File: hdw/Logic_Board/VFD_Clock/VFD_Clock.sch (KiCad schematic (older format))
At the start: 0 parts

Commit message: More work, project restructuring
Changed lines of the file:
@@
 $Descr A 11000 8500
 encoding utf-8
-Sheet 1 14
-Title ""
-Date ""
-Rev ""
-Comp ""
+Sheet 1 19
+Title "VFD Clock"
+Date "2019-04-11"
+Rev "A"
+Comp "Drew Maatman"
 Comment1 ""
 Comment2 ""
@@
 $EndSheet
 $Sheet
-S 3690 4410 500  150
+S 3690 4380 500  150
 U 5B3E071A
 F0 "Temperature Sensors" 50
@@
 F1 "POS24_Input.sch" 50
 $EndSheet
+$Sheet
+S 1180 2600 500  150
+U 5CB0BC26
+F0 "Microcontroller Programming" 50
+F1 "Microcontroller_Programming.sch" 50
+$EndSheet
+$Sheet
+S 3690 2930 500  150
+U 5CB7A8BC
+F0 "Status LEDs" 50
+F1 "Status_LEDs.sch" 50
+$EndSheet
+$Sheet
+S 3690 3280 500  150
+U 5CB7A8C3
+F0 "PGOOD LEDs" 50
+F1 "PGOOD_LEDs.sch" 50
+$EndSheet
+$Sheet
+S 6400 4510 500  150
+U 5CB7B79E
+F0 "IO_Connectors" 50
+F1 "IO_Connectors.sch" 50
+$EndSheet
+$Sheet
+S 6400 4860 500  150
+U 5CB8A16A
+F0 "IO Buffers" 50
+F1 "IO_Buffers.sch" 50
+$EndSheet
 $EndSCHEMATC

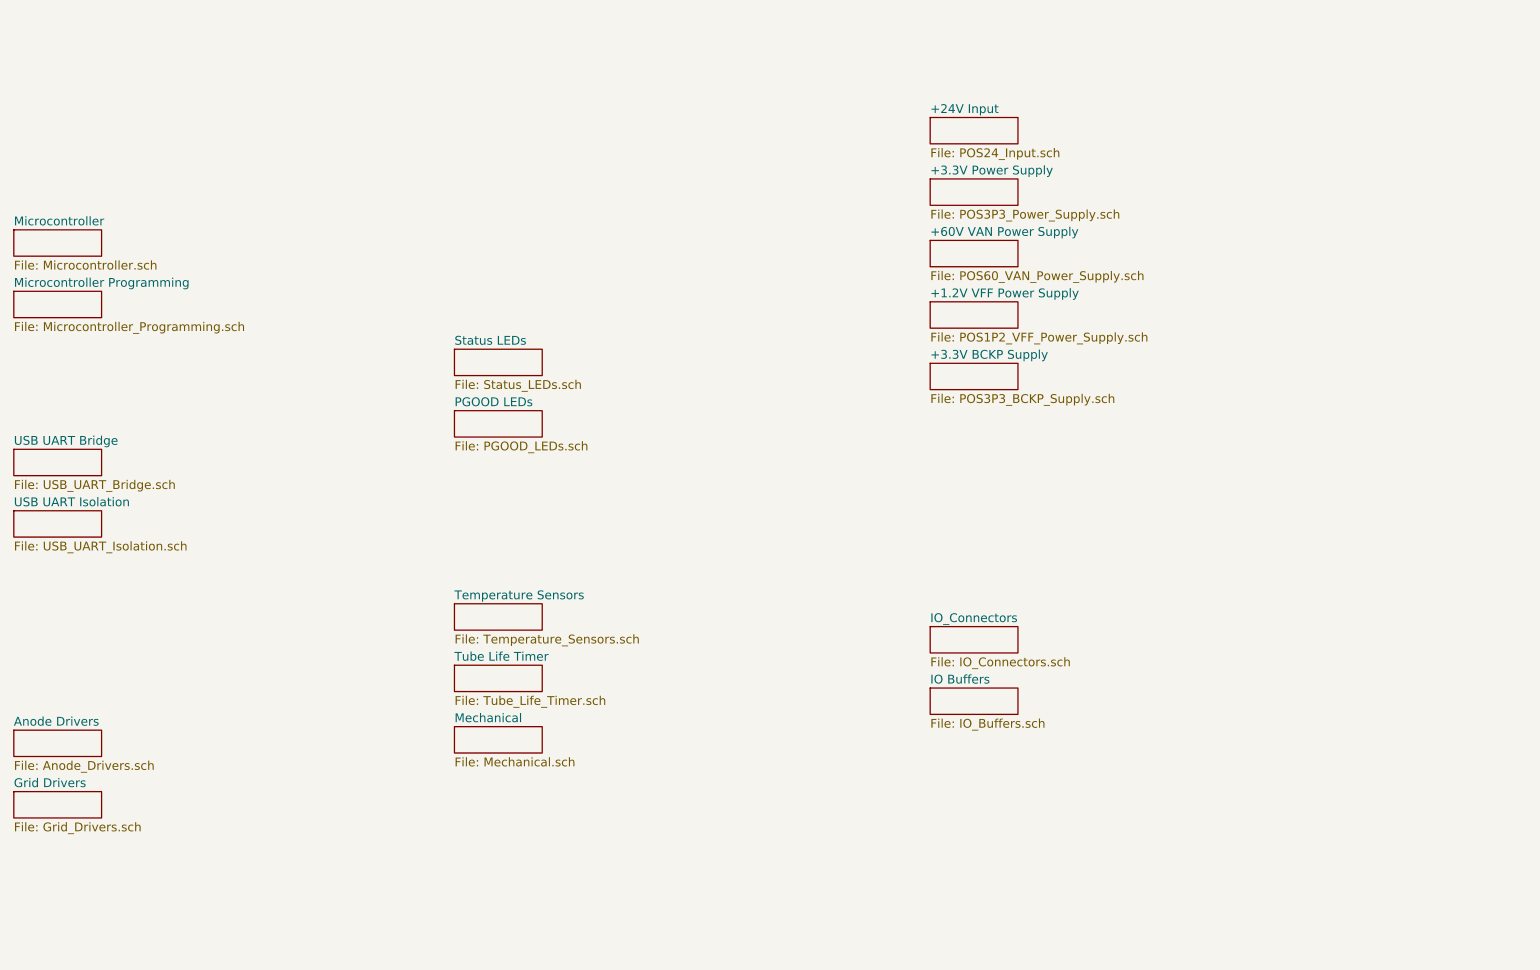
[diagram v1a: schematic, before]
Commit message: Added display board schematic, other additions to logic board
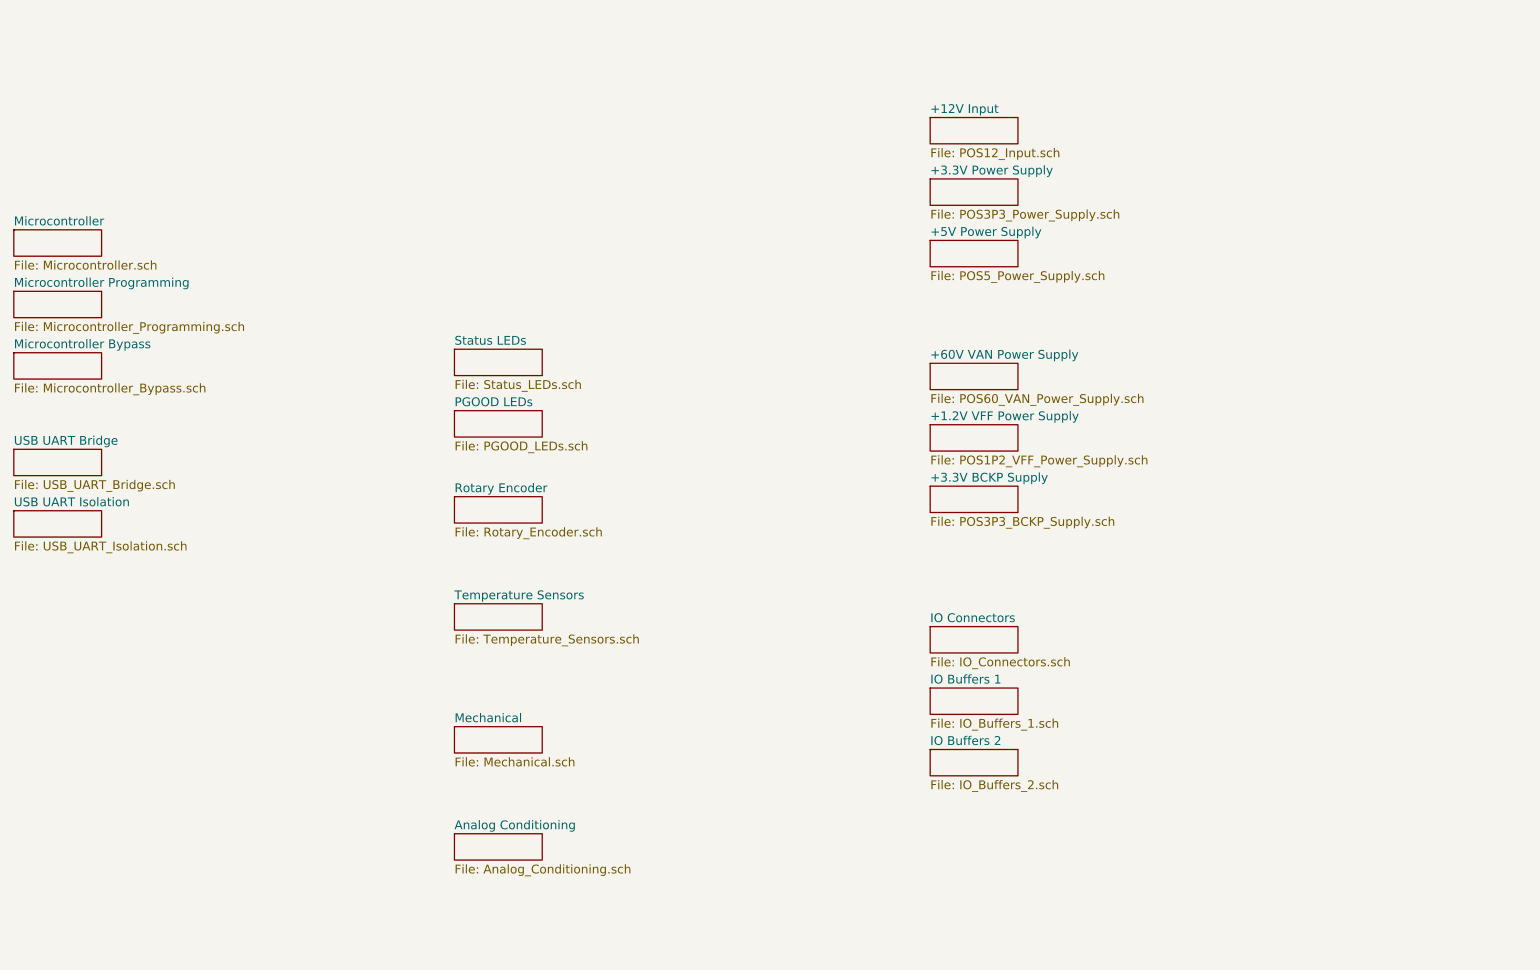
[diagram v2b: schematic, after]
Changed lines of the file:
@@
 $Descr A 11000 8500
 encoding utf-8
-Sheet 1 19
+Sheet 1 21
 Title "VFD Clock"
 Date "2019-04-11"
@@
 $EndSheet
 $Sheet
-S 6400 1960 500  150
-U 5A0B00BA
-F0 "+3.3V Power Supply" 50
-F1 "POS3P3_Power_Supply.sch" 50
-$EndSheet
-$Sheet
-S 6400 2310 500  150
+S 6400 3010 500  150
 U 5A0BC776
 F0 "+60V VAN Power Supply" 50
@@
 $EndSheet
 $Sheet
-S 6400 2660 500  150
+S 6400 3360 500  150
 U 5A0A7E5F
 F0 "+1.2V VFF Power Supply" 50
 F1 "POS1P2_VFF_Power_Supply.sch" 50
-$EndSheet
-$Sheet
-S 1180 5100 500  150
-U 5A2D2FD2
-F0 "Anode Drivers" 50
-F1 "Anode_Drivers.sch" 50
-$EndSheet
-$Sheet
-S 1180 5450 500  150
-U 5A2E3925
-F0 "Grid Drivers" 50
-F1 "Grid_Drivers.sch" 50
 $EndSheet
 $Sheet
@@
 $EndSheet
 $Sheet
-S 3690 4730 500  150
-U 5B4B0915
-F0 "Tube Life Timer" 50
-F1 "Tube_Life_Timer.sch" 50
-$EndSheet
-$Sheet
 S 3690 5080 500  150
 U 5B583C3D
@@
 $EndSheet
 $Sheet
-S 6400 3010 500  150
+S 6400 3710 500  150
 U 5A557C58
 F0 "+3.3V BCKP Supply" 50
@@
 F0 "USB UART Isolation" 50
 F1 "USB_UART_Isolation.sch" 50
-$EndSheet
-$Sheet
-S 6400 1610 500  150
-U 5CB364CC
-F0 "+24V Input" 50
-F1 "POS24_Input.sch" 50
 $EndSheet
 $Sheet
@@
 S 6400 4510 500  150
 U 5CB7B79E
-F0 "IO_Connectors" 50
+F0 "IO Connectors" 50
 F1 "IO_Connectors.sch" 50
 $EndSheet
@@
 S 6400 4860 500  150
 U 5CB8A16A
-F0 "IO Buffers" 50
-F1 "IO_Buffers.sch" 50
+F0 "IO Buffers 1" 50
+F1 "IO_Buffers_1.sch" 50
+$EndSheet
+$Sheet
+S 1180 2950 500  150
+U 5CB25152
+F0 "Microcontroller Bypass" 50
+F1 "Microcontroller_Bypass.sch" 50
+$EndSheet
+$Sheet
+S 6400 1610 500  150
+U 5CB6F1ED
+F0 "+12V Input" 50
+F1 "POS12_Input.sch" 50
+$EndSheet
+$Sheet
+S 6400 1960 500  150
+U 5CB7718D
+F0 "+3.3V Power Supply" 50
+F1 "POS3P3_Power_Supply.sch" 50
+$EndSheet
+$Sheet
+S 3690 3770 500  150
+U 5CC7D654
+F0 "Rotary Encoder" 50
+F1 "Rotary_Encoder.sch" 50
+$EndSheet
+$Sheet
+S 3690 5690 500  150
+U 5CB856E8
+F0 "Analog Conditioning" 50
+F1 "Analog_Conditioning.sch" 50
+$EndSheet
+$Sheet
+S 6400 2310 500  150
+U 5CC14207
+F0 "+5V Power Supply" 50
+F1 "POS5_Power_Supply.sch" 50
+$EndSheet
+$Sheet
+S 6400 5210 500  150
+U 5CC31B3E
+F0 "IO Buffers 2" 50
+F1 "IO_Buffers_2.sch" 50
 $EndSheet
 $EndSCHEMATC

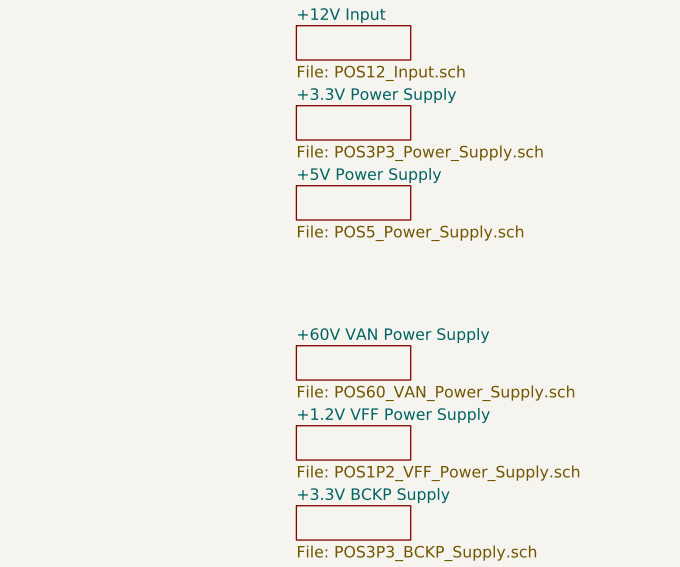
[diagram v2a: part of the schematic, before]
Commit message: Added +3.3V SW sheet
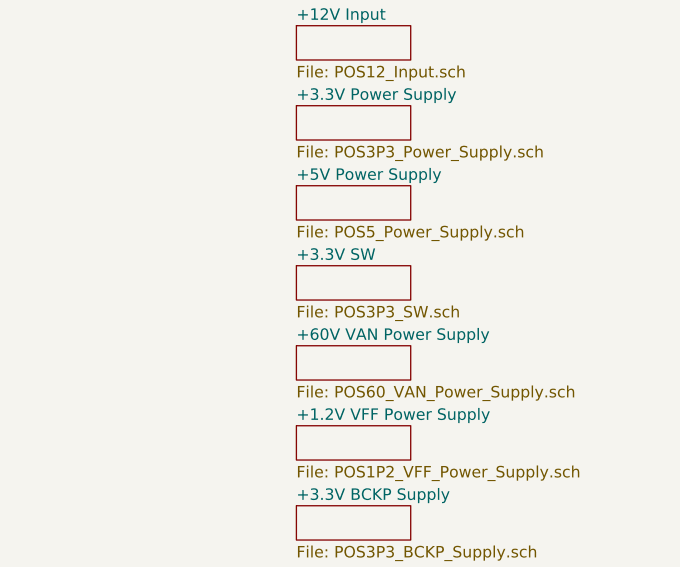
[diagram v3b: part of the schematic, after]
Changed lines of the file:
@@
 $Descr A 11000 8500
 encoding utf-8
-Sheet 1 21
+Sheet 1 22
 Title "VFD Clock"
 Date "2019-04-11"
@@
 F1 "IO_Buffers_2.sch" 50
 $EndSheet
+$Sheet
+S 6400 2660 500  150
+U 5CBB4626
+F0 "+3.3V SW" 50
+F1 "POS3P3_SW.sch" 50
+$EndSheet
 $EndSCHEMATC

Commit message: Resurrected project
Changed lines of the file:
@@
 EESchema Schematic File Version 4
 LIBS:VFD_Clock-cache
-EELAYER 29 0
+EELAYER 30 0
 EELAYER END
 $Descr A 11000 8500
 encoding utf-8
-Sheet 1 22
+Sheet 1 20
 Title "VFD Clock"
 Date "2019-04-11"
@@
 $EndSheet
 $Sheet
-S 3690 4380 500  150
-U 5B3E071A
-F0 "Temperature Sensors" 50
-F1 "Temperature_Sensors.sch" 50
-$EndSheet
-$Sheet
 S 3690 5080 500  150
 U 5B583C3D
@@
 $EndSheet
 $Sheet
-S 1180 3500 500  150
+S 1180 3940 500  150
 U 5CAD2D97
 F0 "USB UART Bridge" 50
@@
 $EndSheet
 $Sheet
-S 1180 3850 500  150
+S 1180 4290 500  150
 U 5CAD2DA3
 F0 "USB UART Isolation" 50
@@
 $EndSheet
 $Sheet
-S 6400 1610 500  150
+S 4780 1120 500  150
 U 5CB6F1ED
 F0 "+12V Input" 50
@@
 F0 "+3.3V Power Supply" 50
 F1 "POS3P3_Power_Supply.sch" 50
-$EndSheet
-$Sheet
-S 3690 3770 500  150
-U 5CC7D654
-F0 "Rotary Encoder" 50
-F1 "Rotary_Encoder.sch" 50
-$EndSheet
-$Sheet
-S 3690 5690 500  150
-U 5CB856E8
-F0 "Analog Conditioning" 50
-F1 "Analog_Conditioning.sch" 50
 $EndSheet
 $Sheet
@@
 $EndSheet
 $Sheet
-S 6400 2660 500  150
-U 5CBB4626
-F0 "+3.3V SW" 50
-F1 "POS3P3_SW.sch" 50
+S 4780 1470 500  150
+U 5E0652BA
+F0 "+12V Telemetry" 50
+F1 "POS12_Telemetry.sch" 50
+$EndSheet
+$Sheet
+S 1180 3300 500  150
+U 5E0CF7BC
+F0 "TELEM I2C Buffer" 50
+F1 "TELEM_I2C_Buffer.sch" 50
 $EndSheet
 $EndSCHEMATC

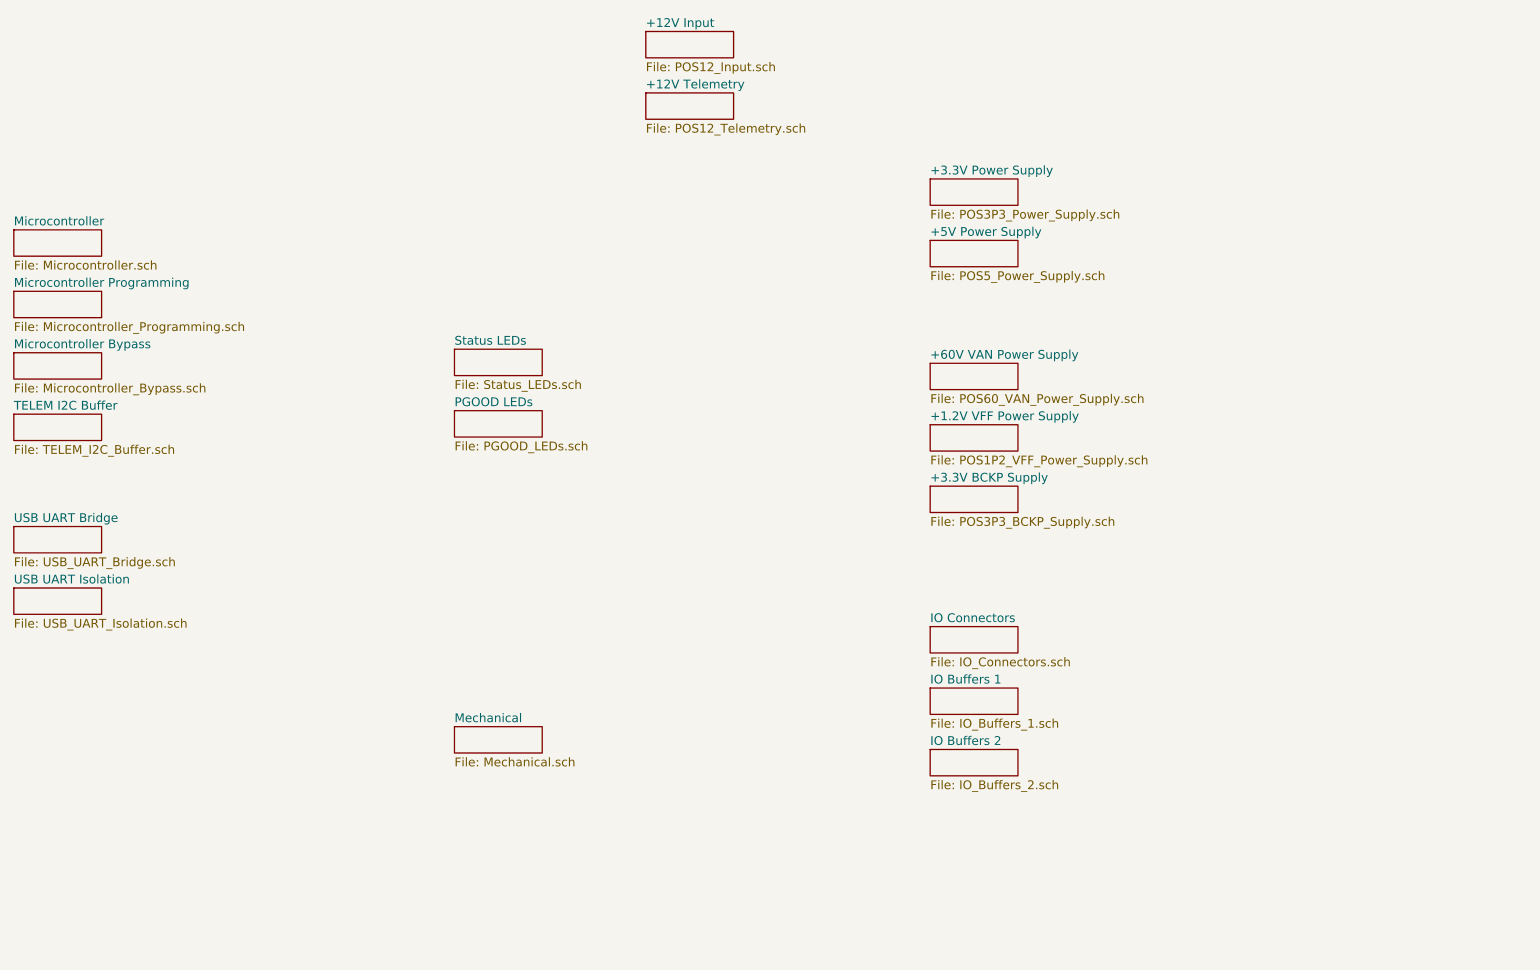
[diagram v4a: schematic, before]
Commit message: Power supply additions
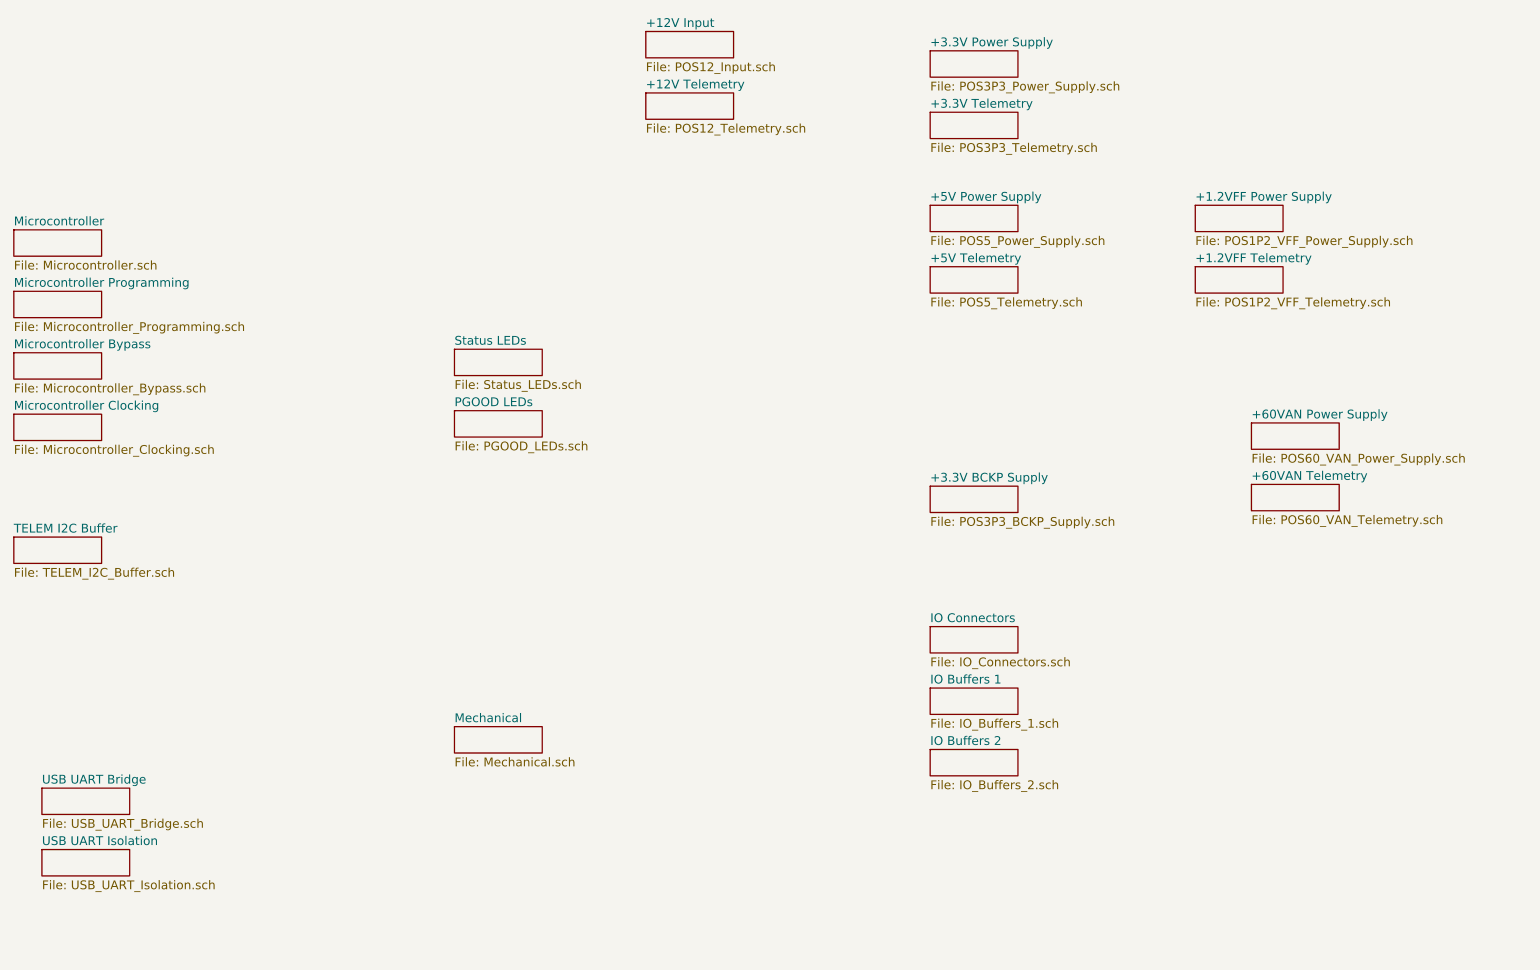
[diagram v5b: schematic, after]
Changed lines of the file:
@@
 $Descr A 11000 8500
 encoding utf-8
-Sheet 1 20
+Sheet 1 25
 Title "VFD Clock"
 Date "2019-04-11"
@@
 $EndSheet
 $Sheet
-S 6400 3010 500  150
+S 8230 3350 500  150
 U 5A0BC776
-F0 "+60V VAN Power Supply" 50
+F0 "+60VAN Power Supply" 50
 F1 "POS60_VAN_Power_Supply.sch" 50
-$EndSheet
-$Sheet
-S 6400 3360 500  150
-U 5A0A7E5F
-F0 "+1.2V VFF Power Supply" 50
-F1 "POS1P2_VFF_Power_Supply.sch" 50
 $EndSheet
 $Sheet
@@
 $EndSheet
 $Sheet
-S 1180 3940 500  150
+S 1340 5430 500  150
 U 5CAD2D97
 F0 "USB UART Bridge" 50
@@
 $EndSheet
 $Sheet
-S 1180 4290 500  150
+S 1340 5780 500  150
 U 5CAD2DA3
 F0 "USB UART Isolation" 50
@@
 $EndSheet
 $Sheet
-S 6400 1960 500  150
+S 6400 1230 500  150
 U 5CB7718D
 F0 "+3.3V Power Supply" 50
 F1 "POS3P3_Power_Supply.sch" 50
-$EndSheet
-$Sheet
-S 6400 2310 500  150
-U 5CC14207
-F0 "+5V Power Supply" 50
-F1 "POS5_Power_Supply.sch" 50
 $EndSheet
 $Sheet
@@
 $EndSheet
 $Sheet
-S 1180 3300 500  150
+S 1180 4000 500  150
 U 5E0CF7BC
 F0 "TELEM I2C Buffer" 50
 F1 "TELEM_I2C_Buffer.sch" 50
 $EndSheet
+$Sheet
+S 1180 3300 500  150
+U 5E01BCC3
+F0 "Microcontroller Clocking" 50
+F1 "Microcontroller_Clocking.sch" 50
+$EndSheet
+$Sheet
+S 6400 1580 500  150
+U 5E0A0E29
+F0 "+3.3V Telemetry" 50
+F1 "POS3P3_Telemetry.sch" 50
+$EndSheet
+$Sheet
+S 6400 2110 500  150
+U 5E0DC082
+F0 "+5V Power Supply" 50
+F1 "POS5_Power_Supply.sch" 50
+$EndSheet
+$Sheet
+S 6400 2460 500  150
+U 5E0DC084
+F0 "+5V Telemetry" 50
+F1 "POS5_Telemetry.sch" 50
+$EndSheet
+$Sheet
+S 7910 2110 500  150
+U 5E0F9110
+F0 "+1.2VFF Power Supply" 50
+F1 "POS1P2_VFF_Power_Supply.sch" 50
+$EndSheet
+$Sheet
+S 7910 2460 500  150
+U 5E0F9112
+F0 "+1.2VFF Telemetry" 50
+F1 "POS1P2_VFF_Telemetry.sch" 50
+$EndSheet
+$Sheet
+S 8230 3700 500  150
+U 5E164364
+F0 "+60VAN Telemetry" 50
+F1 "POS60_VAN_Telemetry.sch" 50
+$EndSheet
 $EndSCHEMATC

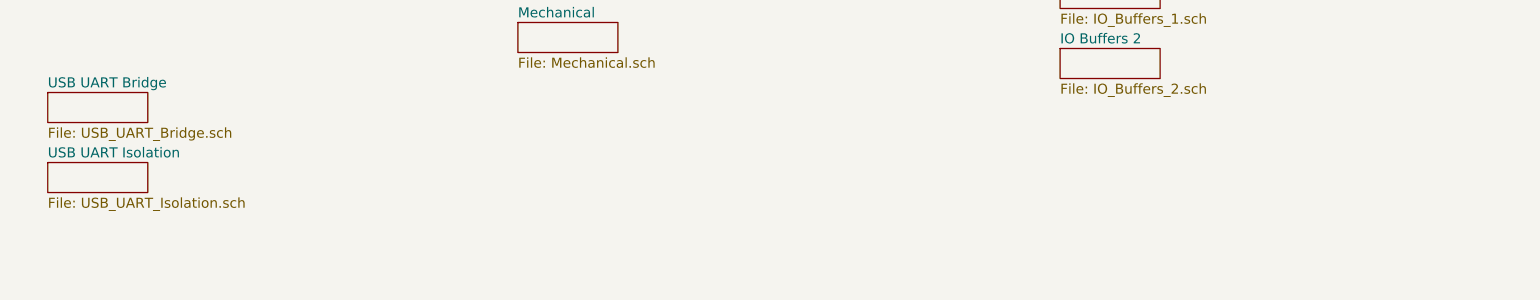
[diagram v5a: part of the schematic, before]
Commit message: Added USB telemetry, isolation, and POS60_VAN current sense
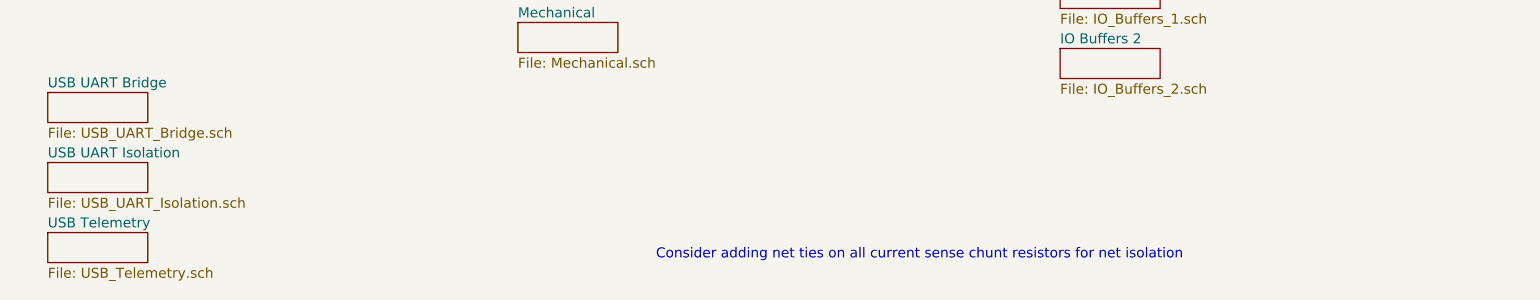
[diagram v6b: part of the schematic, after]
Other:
- note added: "Consider adding net ties on all current sense chunt resistors for net isolation"
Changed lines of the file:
@@
 $Descr A 11000 8500
 encoding utf-8
-Sheet 1 25
+Sheet 1 26
 Title "VFD Clock"
 Date "2019-04-11"
@@
 F1 "POS60_VAN_Telemetry.sch" 50
 $EndSheet
+$Sheet
+S 1340 6130 500  150
+U 5E052856
+F0 "USB Telemetry" 50
+F1 "USB_Telemetry.sch" 50
+$EndSheet
+Text Notes 4380 6270 0    50   ~ 0
+Consider adding net ties on all current sense chunt resistors for net isolation
 $EndSCHEMATC
